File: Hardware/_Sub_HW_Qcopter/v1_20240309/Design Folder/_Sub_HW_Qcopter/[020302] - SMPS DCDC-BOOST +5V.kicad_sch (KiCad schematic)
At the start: 11 parts, among them U3301 TPS613222ADBVR

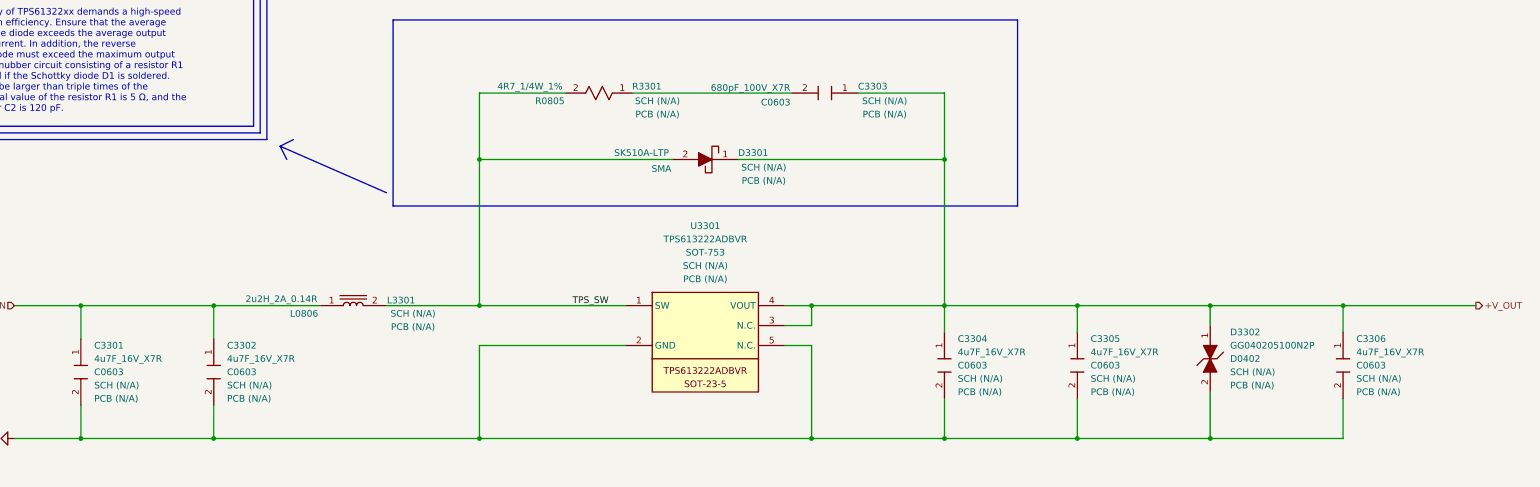
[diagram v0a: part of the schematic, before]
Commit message: Update [020302] - SMPS DCDC-BOOST +5V.kicad_sch
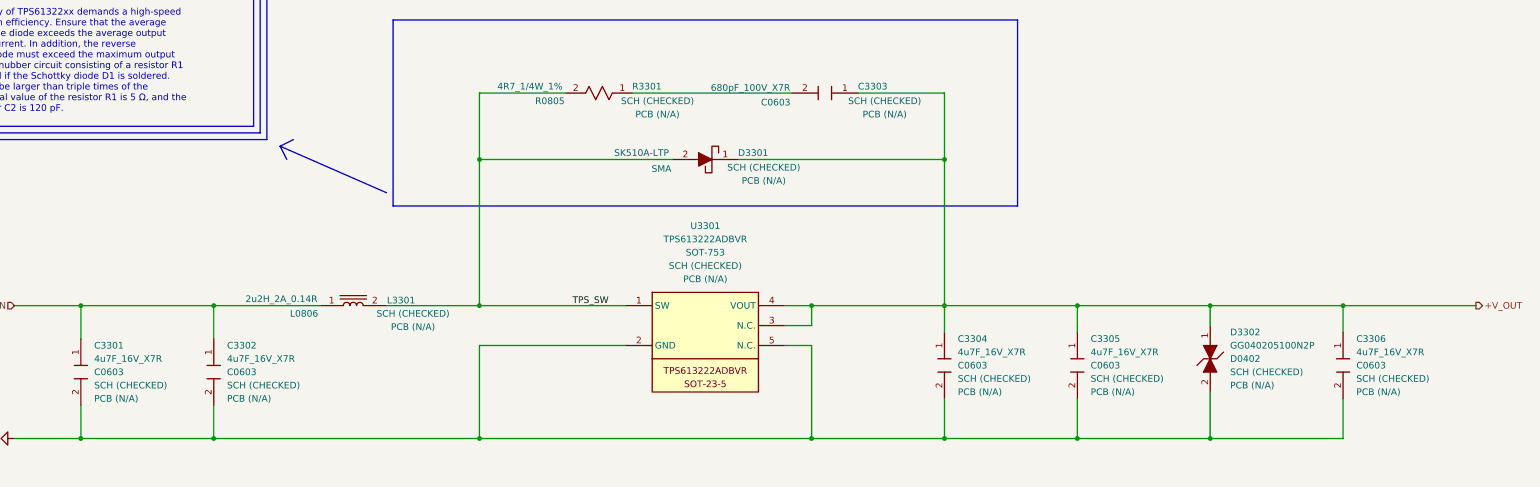
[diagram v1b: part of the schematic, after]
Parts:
- C3301, C3302, C3303, C3304, C3305, C3306, D3301, D3302, L3301, R3301, U3301: SCH CHECK SCH (N/A) -> SCH (CHECKED)
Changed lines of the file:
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@@
 			)
 		)
-		(property "SCH CHECK" "SCH (N/A)"
+		(property "SCH CHECK" "SCH (CHECKED)"
 			(at 306.07 164.084 0)
 			(effects
@@
 			)
 		)
-		(property "SCH CHECK" "SCH (N/A)"
+		(property "SCH CHECK" "SCH (CHECKED)"
 			(at 215.9 204.724 0)
 			(effects
@@
 			)
 		)
-		(property "SCH CHECK" "SCH (N/A)"
+		(property "SCH CHECK" "SCH (CHECKED)"
 			(at 154.94 218.4399 90)
 			(effects
@@
 			)
 		)
-		(property "SCH CHECK" "SCH (N/A)"
+		(property "SCH CHECK" "SCH (CHECKED)"
 			(at 262.636 164.084 0)
 			(effects
@@
 			)
 		)
-		(property "SCH CHECK" "SCH (N/A)"
+		(property "SCH CHECK" "SCH (CHECKED)"
 			(at 180.34 218.4399 90)
 			(effects
@@
 			)
 		)
-		(property "SCH CHECK" "SCH (N/A)"
+		(property "SCH CHECK" "SCH (CHECKED)"
 			(at 282.956 176.784 0)
 			(effects
@@
 			)
 		)
-		(property "SCH CHECK" "SCH (N/A)"
+		(property "SCH CHECK" "SCH (CHECKED)"
 			(at 320.04 217.1699 90)
 			(effects
@@
 			)
 		)
-		(property "SCH CHECK" "SCH (N/A)"
+		(property "SCH CHECK" "SCH (CHECKED)"
 			(at 372.11 215.8999 90)
 			(effects
@@
 			)
 		)
-		(property "SCH CHECK" "SCH (N/A)"
+		(property "SCH CHECK" "SCH (CHECKED)"
 			(at 345.44 217.1699 90)
 			(effects
@@
 			)
 		)
-		(property "SCH CHECK" "SCH (N/A)"
+		(property "SCH CHECK" "SCH (CHECKED)"
 			(at 396.24 217.1699 90)
 			(effects
@@
 			)
 		)
-		(property "SCH CHECK" "SCH (N/A)"
+		(property "SCH CHECK" "SCH (CHECKED)"
 			(at 271.78 195.58 0)
 			(effects

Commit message: Update [020302] - SMPS DCDC-BOOST +5V.kicad_sch
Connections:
- net +V_OUT: now also U3301.5 (N.C.); no longer U3301.3 (N.C.)
- net GND: now also U3301.3 (N.C.); no longer U3301.5 (N.C.)
